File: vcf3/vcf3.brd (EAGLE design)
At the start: 58.4 x 216.8 mm, 99 parts, among them IC1 OPA4130P, IC2 OPA4130P, IC3 OPA134P, Q1 2N3904, Q10 2N3904, Q11 2N3904, Q12 2N3904, Q2 2N3904, Q3 2N3904, Q4 2N3904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

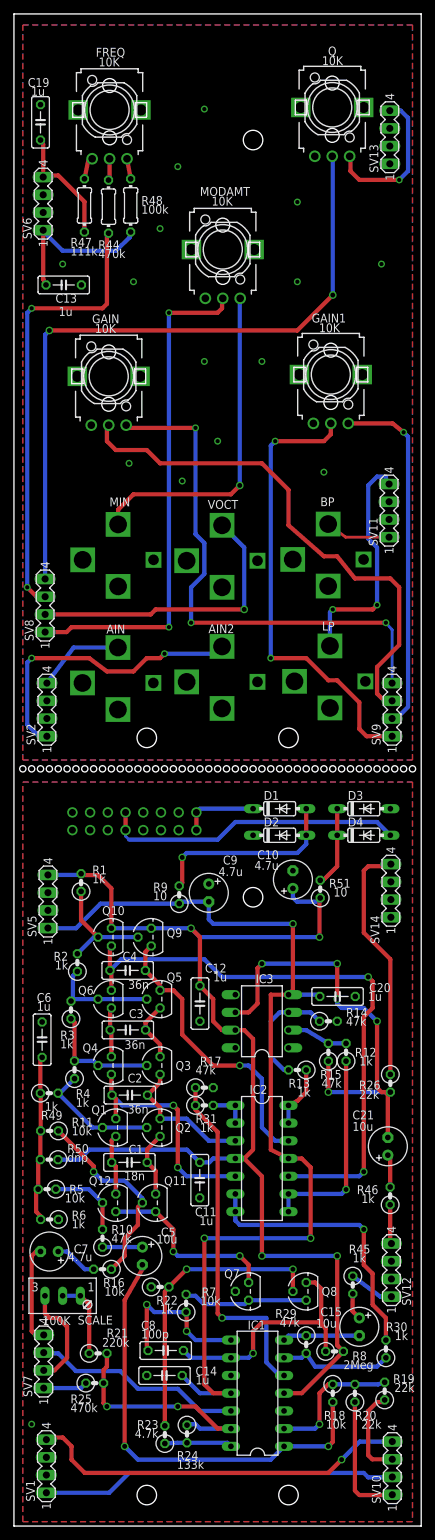
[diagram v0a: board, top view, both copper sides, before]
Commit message: fixed the header position in vcf3 and fixed the 2 pole polarity
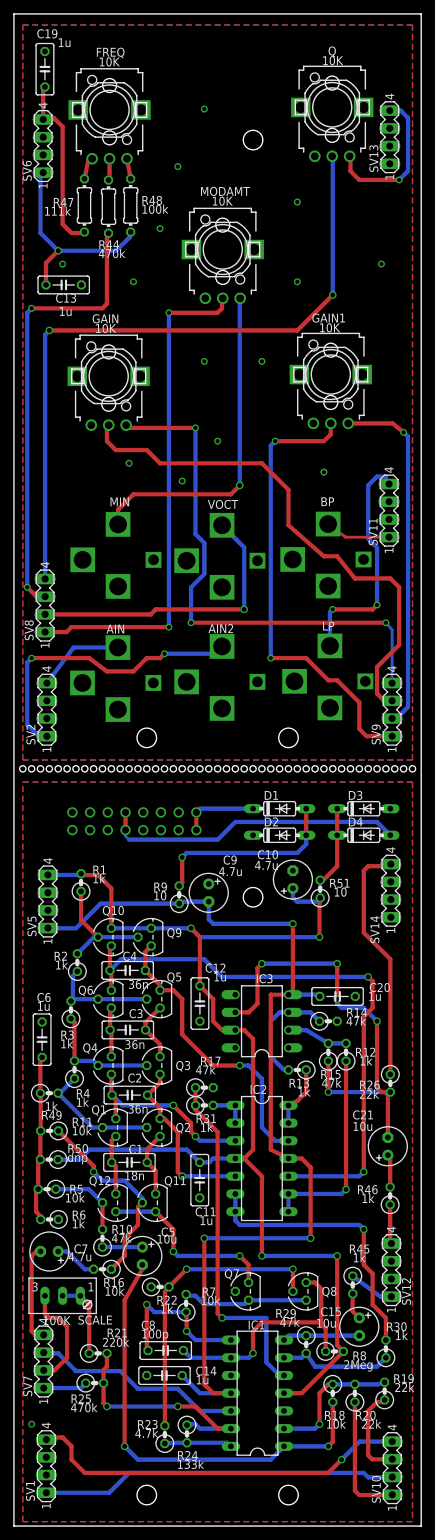
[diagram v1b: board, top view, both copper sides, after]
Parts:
- moved SV6 8.25 mm to (4.19, 197.9)
- moved C19 7.65 mm to (4.45, 208.9)
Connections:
- net N$3: now also IC2.3; no longer IC2.5
- net N$6: now also IC2.5; no longer IC2.3
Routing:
- net +12V: track 193.3 -> 202.0 mm
- net -12V: track 167.8 -> 174.4 mm, vias 3 -> 4
- net N$3: track 33.9 -> 27.7 mm
- net N$6: track 20.0 -> 25.4 mm, vias 0 -> 1
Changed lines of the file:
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@@
 <attribute name="VALUE" x="26.035" y="20.32" size="1.27" layer="21" font="vector" ratio="15"/>
 </element>
-<element name="C19" library="dan" package="C050-025X075" value="1u" x="3.81" y="201.295" smashed="yes" rot="R90">
-<attribute name="NAME" x="5.08" y="207.645" size="1.27" layer="21" font="vector" ratio="15" rot="R180"/>
-<attribute name="VALUE" x="4.445" y="206.375" size="1.27" layer="21" font="vector" ratio="15" rot="R180"/>
+<element name="C19" library="dan" package="C050-025X075" value="1u" x="4.445" y="208.915" smashed="yes" rot="R90">
+<attribute name="NAME" x="6.35" y="214.63" size="1.27" layer="21" font="vector" ratio="15" rot="R180"/>
+<attribute name="VALUE" x="8.255" y="213.36" size="1.27" layer="21" font="vector" ratio="15" rot="R180"/>
 </element>
 <element name="C20" library="dan" package="C050-025X075" value="1u" x="46.4058" y="75.946" smashed="yes">
@@
 </element>
 <element name="R47" library="dan" package="0204/7" value="111k" x="10.1092" y="189.3824" smashed="yes" rot="R270">
-<attribute name="NAME" x="8.1026" y="183.4642" size="1.27" layer="21" font="vector" ratio="15"/>
-<attribute name="VALUE" x="8.1026" y="182.1942" size="1.27" layer="21" font="vector" ratio="15"/>
+<attribute name="NAME" x="5.5626" y="189.1792" size="1.27" layer="21" font="vector" ratio="15"/>
+<attribute name="VALUE" x="4.2926" y="187.9092" size="1.27" layer="21" font="vector" ratio="15"/>
 </element>
 <element name="R48" library="dan" package="0204/7" value="100k" x="16.7386" y="189.3824" smashed="yes" rot="R90">
@@
 <attribute name="VALUE" x="3.2258" y="90.1954" size="1.27" layer="27" ratio="10" rot="R90"/>
 </element>
-<element name="SV6" library="dan" package="MA04-1" value="" x="4.191" y="189.6364" smashed="yes" rot="R90">
-<attribute name="OC_NEWARK" value="unknown" x="4.191" y="189.6364" size="1.778" layer="27" rot="R90" display="off"/>
-<attribute name="MPN" value="" x="4.191" y="189.6364" size="1.778" layer="27" rot="R90" display="off"/>
-<attribute name="MF" value="" x="4.191" y="189.6364" size="1.778" layer="27" rot="R90" display="off"/>
-<attribute name="OC_FARNELL" value="unknown" x="4.191" y="189.6364" size="1.778" layer="27" rot="R90" display="off"/>
-<attribute name="NAME" x="2.54" y="184.5564" size="1.27" layer="21" font="vector" ratio="15" rot="R90"/>
-<attribute name="VALUE" x="2.54" y="190.2714" size="1.27" layer="27" ratio="10" rot="R90"/>
+<element name="SV6" library="dan" package="MA04-1" value="" x="4.191" y="197.8914" smashed="yes" rot="R90">
+<attribute name="OC_NEWARK" value="unknown" x="4.191" y="197.8914" size="1.778" layer="27" rot="R90" display="off"/>
+<attribute name="MPN" value="" x="4.191" y="197.8914" size="1.778" layer="27" rot="R90" display="off"/>
+<attribute name="MF" value="" x="4.191" y="197.8914" size="1.778" layer="27" rot="R90" display="off"/>
+<attribute name="OC_FARNELL" value="unknown" x="4.191" y="197.8914" size="1.778" layer="27" rot="R90" display="off"/>
+<attribute name="NAME" x="2.54" y="192.8114" size="1.27" layer="21" font="vector" ratio="15" rot="R90"/>
+<attribute name="VALUE" x="2.54" y="198.5264" size="1.27" layer="27" ratio="10" rot="R90"/>
 </element>
 <element name="SV7" library="dan" package="MA04-1" value="" x="4.2672" y="23.5966" smashed="yes" rot="R90">
@@
 <signal name="N$3">
 <contactref element="C2" pad="1"/>
-<contactref element="IC2" pad="5"/>
 <contactref element="Q1" pad="1"/>
 <contactref element="Q4" pad="3"/>
@@
 <wire x1="13.97" y1="64.77" x2="13.97" y2="61.8998" width="0.6096" layer="1"/>
 <wire x1="13.97" y1="61.8998" x2="14.0716" y2="61.7982" width="0.6096" layer="1"/>
-<wire x1="31.75" y1="50.165" x2="24.765" y2="50.165" width="0.6096" layer="16"/>
-<wire x1="24.765" y1="50.165" x2="23.495" y2="51.435" width="0.6096" layer="16"/>
-<via x="23.495" y="51.435" extent="1-16" drill="0.7"/>
-<wire x1="23.495" y1="51.435" x2="23.495" y2="59.69" width="0.6096" layer="1"/>
-<wire x1="23.495" y1="59.69" x2="22.86" y2="60.325" width="0.6096" layer="1"/>
+<wire x1="25.4" y1="57.785" x2="22.86" y2="60.325" width="0.6096" layer="1"/>
 <via x="22.86" y="60.325" extent="1-16" drill="0.7"/>
 <wire x1="22.86" y1="60.325" x2="15.5448" y2="60.325" width="0.6096" layer="16"/>
 <wire x1="15.5448" y1="60.325" x2="14.0716" y2="61.7982" width="0.6096" layer="16"/>
+<contactref element="IC2" pad="3"/>
+<wire x1="25.4" y1="57.785" x2="25.4" y2="56.515" width="0.6096" layer="1"/>
+<wire x1="25.4" y1="56.515" x2="26.035" y2="55.88" width="0.6096" layer="1"/>
+<via x="26.035" y="55.88" extent="1-16" drill="0.7"/>
+<wire x1="26.035" y1="55.88" x2="26.67" y2="55.245" width="0.6096" layer="16"/>
+<wire x1="26.67" y1="55.245" x2="31.75" y2="55.245" width="0.6096" layer="16"/>
 </signal>
 <signal name="N$4">
@@
 <signal name="N$6">
 <contactref element="C2" pad="2"/>
-<contactref element="IC2" pad="3"/>
 <contactref element="Q2" pad="1"/>
 <contactref element="Q3" pad="3"/>
@@
 <wire x1="20.955" y1="64.77" x2="20.955" y2="63.6016" width="0.6096" layer="1"/>
 <wire x1="20.955" y1="63.6016" x2="19.1516" y2="61.7982" width="0.6096" layer="1"/>
-<wire x1="31.75" y1="55.245" x2="27.94" y2="55.245" width="0.6096" layer="16"/>
-<wire x1="27.94" y1="55.245" x2="24.765" y2="58.42" width="0.6096" layer="16"/>
-<wire x1="24.765" y1="58.42" x2="20.955" y2="58.42" width="0.6096" layer="16"/>
+<contactref element="IC2" pad="5"/>
+<wire x1="20.955" y1="58.42" x2="21.59" y2="58.42" width="0.6096" layer="1"/>
+<wire x1="21.59" y1="58.42" x2="23.495" y2="56.515" width="0.6096" layer="1"/>
+<wire x1="23.495" y1="56.515" x2="23.495" y2="50.8" width="0.6096" layer="1"/>
+<wire x1="23.495" y1="50.8" x2="24.13" y2="50.165" width="0.6096" layer="1"/>
+<via x="24.13" y="50.165" extent="1-16" drill="0.7"/>
+<wire x1="24.13" y1="50.165" x2="31.75" y2="50.165" width="0.6096" layer="16"/>
 </signal>
 <signal name="N$7">
@@
 <contactref element="SV6" pad="4"/>
 <contactref element="SV5" pad="4"/>
-<wire x1="4.191" y1="193.4464" x2="4.191" y2="198.159" width="0.6096" layer="1"/>
-<wire x1="4.191" y1="198.159" x2="3.81" y2="198.755" width="0.6096" layer="1"/>
+<wire x1="4.191" y1="201.7014" x2="4.191" y2="205.779" width="0.6096" layer="1"/>
+<wire x1="4.191" y1="205.779" x2="4.445" y2="206.375" width="0.6096" layer="1"/>
 <contactref element="IC1" pad="4"/>
 <contactref element="IC2" pad="4"/>
@@
 <wire x1="43.815" y1="89.9668" x2="43.9166" y2="90.0684" width="0.6096" layer="1"/>
 <contactref element="R47" pad="2"/>
-<wire x1="10.1092" y1="185.5724" x2="10.1092" y2="189.9158" width="0.6096" layer="1"/>
-<wire x1="10.1092" y1="189.9158" x2="6.35" y2="193.675" width="0.6096" layer="1"/>
-<wire x1="6.35" y1="193.675" x2="4.4196" y2="193.675" width="0.6096" layer="1"/>
-<wire x1="4.4196" y1="193.675" x2="4.191" y2="193.4464" width="0.6096" layer="1"/>
+<wire x1="10.1092" y1="185.5724" x2="10.1092" y2="185.4708" width="0.6096" layer="1"/>
+<wire x1="5.715" y1="201.93" x2="4.4196" y2="201.93" width="0.6096" layer="1"/>
+<wire x1="4.4196" y1="201.93" x2="4.191" y2="201.7014" width="0.6096" layer="1"/>
 <wire x1="13.97" y1="91.44" x2="12.065" y2="93.345" width="0.6096" layer="1"/>
 <wire x1="12.065" y1="93.345" x2="9.8298" y2="93.345" width="0.6096" layer="1"/>
@@
 <wire x1="47.244" y1="25.0444" x2="47.244" y2="25.019" width="0.6096" layer="1"/>
 <wire x1="47.244" y1="25.019" x2="41.275" y2="19.05" width="0.6096" layer="1"/>
-<wire x1="9.6266" y1="93.5482" x2="10.1092" y2="185.5724" width="0" layer="19" extent="16-16"/>
+<wire x1="10.1092" y1="185.4708" x2="10.16" y2="185.42" width="0.6096" layer="1"/>
+<wire x1="10.16" y1="185.42" x2="8.255" y2="185.42" width="0.6096" layer="1"/>
+<wire x1="8.255" y1="185.42" x2="6.985" y2="186.69" width="0.6096" layer="1"/>
+<wire x1="6.985" y1="186.69" x2="6.985" y2="200.66" width="0.6096" layer="1"/>
+<wire x1="6.985" y1="200.66" x2="5.715" y2="201.93" width="0.6096" layer="1"/>
+<wire x1="9.6266" y1="93.5482" x2="10.16" y2="185.42" width="0" layer="19" extent="1-16"/>
 </signal>
 <signal name="-12V">
@@
 <contactref element="SV5" pad="1"/>
 <contactref element="SV6" pad="1"/>
-<wire x1="4.191" y1="185.8264" x2="4.6736" y2="185.1914" width="0.4064" layer="16"/>
-<wire x1="4.6736" y1="185.1914" x2="6.985" y2="182.88" width="0.6096" layer="16"/>
-<wire x1="6.985" y1="182.88" x2="14.605" y2="182.88" width="0.6096" layer="16"/>
-<wire x1="4.191" y1="185.8264" x2="4.191" y2="178.8042" width="0.6096" layer="1"/>
-<wire x1="4.191" y1="178.8042" x2="4.5974" y2="177.9778" width="0.6096" layer="1"/>
+<wire x1="6.35" y1="182.88" x2="14.605" y2="182.88" width="0.6096" layer="16"/>
 <contactref element="IC1" pad="11"/>
 <contactref element="IC2" pad="11"/>
@@
 <wire x1="42.545" y1="51.435" x2="41.275" y2="52.705" width="0.6096" layer="1"/>
 <wire x1="41.275" y1="52.705" x2="39.37" y2="52.705" width="0.6096" layer="1"/>
+<wire x1="3.81" y1="185.42" x2="3.81" y2="193.7004" width="0.6096" layer="16"/>
+<wire x1="3.81" y1="193.7004" x2="4.191" y2="194.0814" width="0.6096" layer="16"/>
+<wire x1="4.5974" y1="177.9778" x2="4.5974" y2="181.1274" width="0.6096" layer="1"/>
+<wire x1="4.5974" y1="181.1274" x2="6.35" y2="182.88" width="0.6096" layer="1"/>
+<via x="6.35" y="182.88" extent="1-16" drill="0.7"/>
+<wire x1="6.35" y1="182.88" x2="3.81" y2="185.42" width="0.6096" layer="16"/>
 <wire x1="12.4206" y1="89.2556" x2="4.5974" y2="177.9778" width="0" layer="19" extent="16-16"/>
 </signal>

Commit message: added center freq trimpot to vcf3, fixed v/oct tracking
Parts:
- added CENTER: 20K, dan:S64W
- R21: value 220k -> 1M
- R47: value 111k -> 91k
- SCALE: value 100K -> 500K
- moved C19 26.2 mm to (7.62, 182.9), turned to 180 degrees
- moved SV5 5.72 mm to (4.88, 83.8)
- moved R1 4.62 mm to (8.36, 87.8)
- moved SV6 4.44 mm to (4.19, 193.4)
- moved R2 1.42 mm to (10.4, 80.2)
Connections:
- new net N$40: C19.1, CENTER.E, CENTER.S, R47.2, SV5.4, SV6.4
- net +12V: now also CENTER.A; no longer C19.1, R47.2, SV5.4, SV6.4
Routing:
- net N$40: track 0.00 -> 28.1 mm
- net +12V: track 202.0 -> 175.1 mm
- net N$10: track 17.2 -> 14.2 mm
- net -12V: track 174.4 -> 176.2 mm

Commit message: fixed the levels for the 3340 and vcf3
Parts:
- R18: value 10k -> 1k
- R19, R20: value 22k -> 47k
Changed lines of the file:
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@@
 <attribute name="VALUE" x="26.035" y="64.77" size="1.27" layer="21" font="vector" ratio="15"/>
 </element>
-<element name="R18" library="dan" package="0207/2V" value="10k" x="45.72" y="19.05" smashed="yes" rot="R270">
+<element name="R18" library="dan" package="0207/2V" value="1k" x="45.72" y="19.05" smashed="yes" rot="R270">
 <attribute name="NAME" x="44.45" y="15.24" size="1.27" layer="21" font="vector" ratio="15"/>
 <attribute name="VALUE" x="47.625" y="15.24" size="1.27" layer="21" font="vector" ratio="15" rot="R180"/>
 </element>
-<element name="R19" library="dan" package="0207/2V" value="22k" x="53.1622" y="19.3548" smashed="yes" rot="R90">
+<element name="R19" library="dan" package="0207/2V" value="47k" x="53.1622" y="19.3548" smashed="yes" rot="R90">
 <attribute name="NAME" x="57.4548" y="21.7678" size="1.27" layer="21" font="vector" ratio="15" rot="R180"/>
 <attribute name="VALUE" x="57.4548" y="20.4978" size="1.27" layer="21" font="vector" ratio="15" rot="R180"/>
@@
 <attribute name="VALUE" x="9.6774" y="81.0768" size="1.27" layer="21" font="vector" ratio="15" rot="R180"/>
 </element>
-<element name="R20" library="dan" package="0207/2V" value="22k" x="48.895" y="19.05" smashed="yes" rot="R90">
+<element name="R20" library="dan" package="0207/2V" value="47k" x="48.895" y="19.05" smashed="yes" rot="R90">
 <attribute name="NAME" x="48.895" y="15.24" size="1.27" layer="21" font="vector" ratio="15"/>
 <attribute name="VALUE" x="52.705" y="15.24" size="1.27" layer="21" font="vector" ratio="15" rot="R180"/>

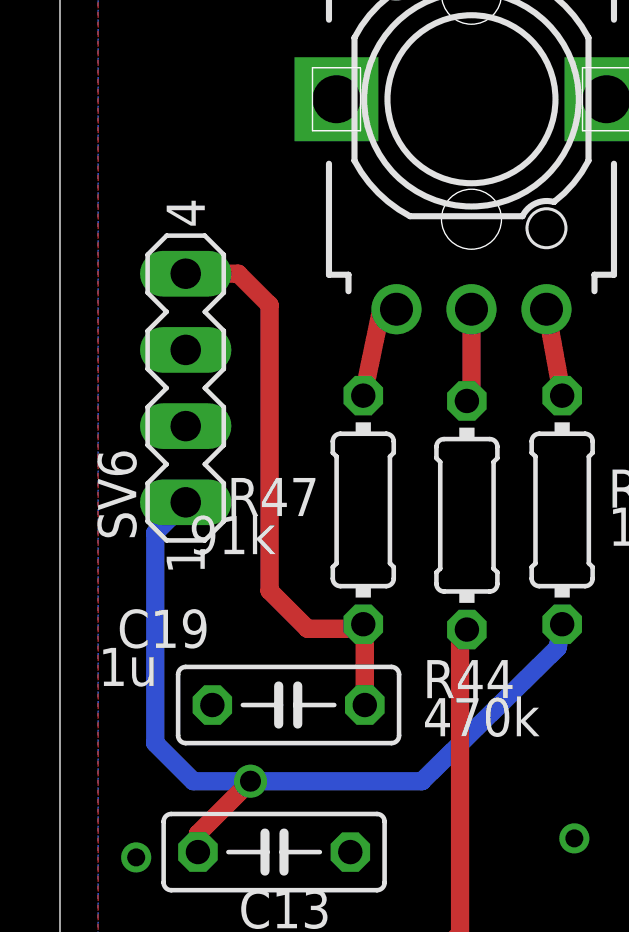
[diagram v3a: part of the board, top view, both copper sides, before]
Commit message: sent out vcf3 and 3320 for re spin
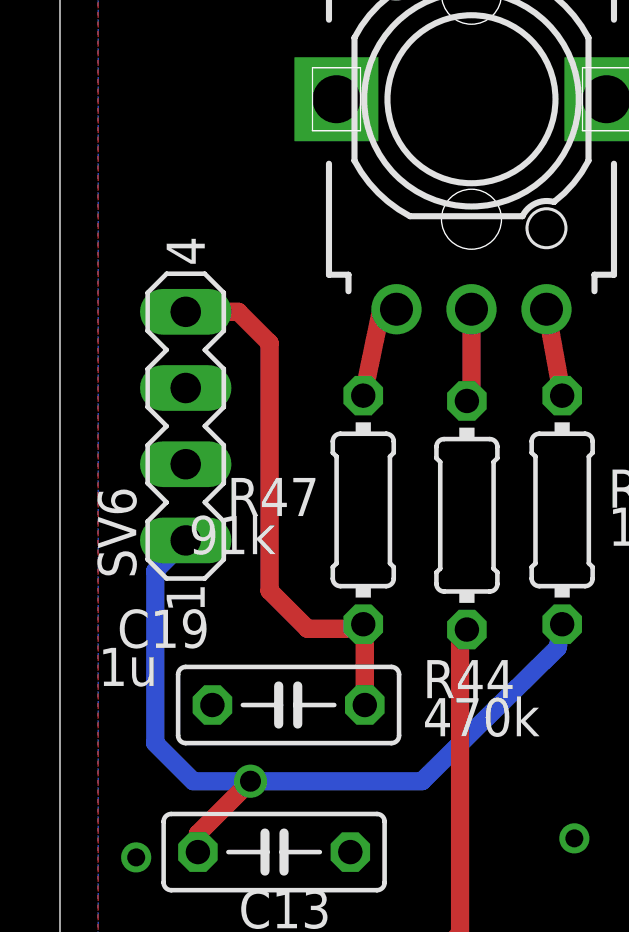
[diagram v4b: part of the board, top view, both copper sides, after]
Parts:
- moved SV6 1.27 mm to (4.19, 192.2)
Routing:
- net N$40: track 28.1 -> 26.9 mm
- net -12V: track 176.2 -> 174.9 mm
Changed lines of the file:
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@@
 <layer number="19" name="Unrouted" color="6" fill="1" visible="yes" active="yes"/>
 <layer number="20" name="Dimension" color="15" fill="1" visible="yes" active="yes"/>
-<layer number="21" name="tPlace" color="7" fill="1" visible="yes" active="yes"/>
-<layer number="22" name="bPlace" color="7" fill="1" visible="yes" active="yes"/>
+<layer number="21" name="tPlace" color="7" fill="1" visible="no" active="yes"/>
+<layer number="22" name="bPlace" color="7" fill="1" visible="no" active="yes"/>
 <layer number="23" name="tOrigins" color="15" fill="1" visible="yes" active="yes"/>
 <layer number="24" name="bOrigins" color="15" fill="1" visible="yes" active="yes"/>
@@
 <attribute name="VALUE" x="3.2258" y="84.4804" size="1.27" layer="27" ratio="10" rot="R90"/>
 </element>
-<element name="SV6" library="dan" package="MA04-1" value="" x="4.191" y="193.4464" smashed="yes" rot="R90">
-<attribute name="OC_NEWARK" value="unknown" x="4.191" y="193.4464" size="1.778" layer="27" rot="R90" display="off"/>
-<attribute name="MPN" value="" x="4.191" y="193.4464" size="1.778" layer="27" rot="R90" display="off"/>
-<attribute name="MF" value="" x="4.191" y="193.4464" size="1.778" layer="27" rot="R90" display="off"/>
-<attribute name="OC_FARNELL" value="unknown" x="4.191" y="193.4464" size="1.778" layer="27" rot="R90" display="off"/>
-<attribute name="NAME" x="2.54" y="188.3664" size="1.27" layer="21" font="vector" ratio="15" rot="R90"/>
-<attribute name="VALUE" x="2.54" y="194.0814" size="1.27" layer="27" ratio="10" rot="R90"/>
+<element name="SV6" library="dan" package="MA04-1" value="" x="4.191" y="192.1764" smashed="yes" rot="R90">
+<attribute name="OC_NEWARK" value="unknown" x="4.191" y="192.1764" size="1.778" layer="27" rot="R90" display="off"/>
+<attribute name="MPN" value="" x="4.191" y="192.1764" size="1.778" layer="27" rot="R90" display="off"/>
+<attribute name="MF" value="" x="4.191" y="192.1764" size="1.778" layer="27" rot="R90" display="off"/>
+<attribute name="OC_FARNELL" value="unknown" x="4.191" y="192.1764" size="1.778" layer="27" rot="R90" display="off"/>
+<attribute name="NAME" x="2.54" y="187.0964" size="1.27" layer="21" font="vector" ratio="15" rot="R90"/>
+<attribute name="VALUE" x="2.54" y="192.8114" size="1.27" layer="27" ratio="10" rot="R90"/>
 </element>
 <element name="SV7" library="dan" package="MA04-1" value="" x="4.2672" y="23.5966" smashed="yes" rot="R90">
@@
 <wire x1="6.35" y1="180.34" x2="4.445" y2="180.34" width="0.6096" layer="16"/>
 <wire x1="4.445" y1="180.34" x2="3.175" y2="181.61" width="0.6096" layer="16"/>
-<wire x1="3.175" y1="181.61" x2="3.175" y2="188.6204" width="0.6096" layer="16"/>
-<wire x1="3.175" y1="188.6204" x2="4.191" y2="189.6364" width="0.6096" layer="16"/>
+<wire x1="3.175" y1="181.61" x2="3.175" y2="187.3504" width="0.6096" layer="16"/>
+<wire x1="3.175" y1="187.3504" x2="4.191" y2="188.3664" width="0.6096" layer="16"/>
 <wire x1="4.9022" y1="80.01" x2="6.35" y2="80.01" width="0.6096" layer="16"/>
 <wire x1="6.35" y1="80.01" x2="9.525" y2="83.185" width="0.6096" layer="16"/>
@@
 <contactref element="SV5" pad="4"/>
 <contactref element="CENTER" pad="S"/>
-<wire x1="4.191" y1="197.2564" x2="5.9436" y2="197.2564" width="0.6096" layer="1"/>
-<wire x1="5.9436" y1="197.2564" x2="6.985" y2="196.215" width="0.6096" layer="1"/>
-<wire x1="6.985" y1="196.215" x2="6.985" y2="186.69" width="0.6096" layer="1"/>
+<wire x1="4.191" y1="195.9864" x2="5.9436" y2="195.9864" width="0.6096" layer="1"/>
+<wire x1="5.9436" y1="195.9864" x2="6.985" y2="194.945" width="0.6096" layer="1"/>
+<wire x1="6.985" y1="194.945" x2="6.985" y2="186.69" width="0.6096" layer="1"/>
 <wire x1="6.985" y1="186.69" x2="8.255" y2="185.42" width="0.6096" layer="1"/>
 <wire x1="8.255" y1="185.42" x2="9.9568" y2="185.42" width="0.6096" layer="1"/>
